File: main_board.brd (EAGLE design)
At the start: 100 x 80 mm, 60 parts, among them IC1 MBED_MICROCONTROLLER, J1 2060-402, U11 MC33887-HSOP, U13 MC33887-HSOP, U14 PCF8575PWE4, U2 SI8460AA-B-IS1, U3 MC33887-HSOP, U4 NFET-SOIC8, U5 LDO, U6 SI8460AA-B-IS1, U7 MC33887-HSOP, U8 SI8460AA-B-IS1, U9 MC33887-HSOP, X3 ENC1, X4 ENC2, X6 ENC3, X7 ENC4, X8 ENC5

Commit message: Major changes, nearly ready for first prototype
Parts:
- removed C3: 100nF, rcl:C0603K
- removed J1: 2060-402, Wago-2060-402:WAGO_2060-402
- removed JP1, JP3, JP4, JP5, JP6: MOTOR, SparkFun:SCREWTERMINAL-3.5MM-2
- removed JP2: PWR, SparkFun:SCREWTERMINAL-3.5MM-2
- removed LED4: (no value), led:CHIP-LED0603
- removed R19, R22, R25, R28: 10k, rcl:R0603
- removed U14: PCF8575PWE4, pcf8575:SOP65P640X120-24N
- removed U4: NFET-SOIC8, SparkFun:SO08
- removed U5: LDO, SparkFun:SOT23-5
- added BAT_12V, BAT_GND: (no value), tellis2:PWR_HOLE
- added BAT_15V, BAT_15V_GND, M1_1, M1_10, M1_2, M1_3, M1_4, M1_5, M1_6, M1_7, M1_8, M1_9: (no value), tellis2:WIRE_HOLE
- added LED1, LED2, LED3: (no value), led:CHIP-LED0603
- added R1, R2, R3, R4, R5: 10k, rcl:R0603
- added R14, R7, R8, R9: 2K2, rcl:R0603
- added U$1: V_REG_MIC2920, SparkFun-PowerIC:SOT223
- added U$2: MOSFET-N-SOT669, nxp_sot669:TO127P600X120-5N
- added U$3: D15V35F5S3, D15V35F5S3:D15V35F5S3
- added U1: PCA9555PW,118, PCA9555:SOP65P640X110-24N
- added X1: BALL_SENS, con-amp-micromatch:MICROMATCH-4
- added X10: IMU, con-amp-micromatch:MICROMATCH-4
- added X2: ETH, con-amp-micromatch:MICROMATCH-4
- added X5: BTNS, con-amp-micromatch:MICROMATCH-4
- added X9: COIL, con-amp-micromatch:MICROMATCH-6
- R11: value 10k -> 2K2
- R6: value 1k -> 2K2
- moved R11 176.1 mm to (77.7, 53.5), flipped to the bottom, turned to 180 degrees
- moved R29 155.1 mm to (49.3, 24.9), flipped to the bottom, turned to 90 degrees
- moved C30 151.2 mm to (36.6, 18.6)
- moved R6 144.5 mm to (95.5, 10.0), turned to 90 degrees
- moved C17 139.0 mm to (53.1, 27.2), turned to 270 degrees
- moved R27 137.9 mm to (36.6, 20.2), turned to 180 degrees
- moved R26 134.8 mm to (27.5, 7.31), flipped to the bottom, turned to 180 degrees
- moved C25 132.9 mm to (21.1, 21.2), turned to 270 degrees
- moved C16 131.4 mm to (54.4, 33.4)
- moved C6 130.7 mm to (37.3, 51.7), flipped to the bottom, turned to 270 degrees
- moved C8 130.0 mm to (27.1, 52.4), flipped to the bottom, turned to 270 degrees
- moved D1 128.9 mm to (27.8, 24.7), flipped to the bottom, turned to 180 degrees
- moved C5 123.9 mm to (48.6, 62.5), turned to 180 degrees
- moved R24 114.3 mm to (22.7, 21.3), turned to 90 degrees
- moved C20 113.9 mm to (21.1, 47.9), turned to 270 degrees
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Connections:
- removed net EXTEND_SCL: IC1.10, U14.22
- removed net EXTEND_SDA: IC1.9, U14.23
- removed net N$11: C3.1, U5.4
- removed net N$13: LED4.A, R6.1
- removed net N$17: R11.1, U3.20
- removed net N$32: R19.1, U7.20
- removed net N$37: R22.1, U9.20
- removed net N$42: R25.1, U11.20
- removed net N$47: R28.1, U13.20
- new net +15V: BAT_15V.P$1, U$3.EN, U$3.P$5
- new net BALL: U1.15, X1.2
- new net BTN1: U1.19, X5.2
- new net BTN2: U1.20, X5.4
- new net CHARGE: IC1.20, X9.4
- new net D+: IC1.31
- new net D-: IC1.32
- new net DONE: IC1.18, X9.5
- new net INT: IC1.8, R11.1, U1.1
- new net KICK: IC1.19, X9.3
- new net LED1: R6.2, U1.16
- new net LED2: R7.2, U1.17
- new net LED3: R8.2, U1.18
- new net N$19: X9.6
- new net N$2: R1.1, U3.20
- new net N$3: R2.1, U7.20
- new net N$4: R3.1, U13.20
- new net N$5: R4.1, U11.20
- new net N$6: R5.1, U9.20
- new net N$7: LED1.A, R6.1
- new net N$8: LED2.A, R7.1
- new net N$9: LED3.A, R8.1
- new net RD+: IC1.35, X2.2
- new net RD-: IC1.36, X2.1
- new net SCL: IC1.10, R9.1, U1.22, X10.3
- new net SDA: IC1.9, R14.1, U1.23, X10.4
- new net TD+: IC1.33, X2.4
- new net TD-: IC1.34, X2.3
- net +12V: now also U$1.1; no longer U5.1, U5.3
- net +3V3: now also R11.2, R14.2, R9.2, U1.24, X10.1; no longer U14.24
- net +5V: now also R1.2, R2.2, R3.2, R4.2, R5.2, U$1.3; no longer R11.2, R19.2, R22.2, R25.2, R28.2, R6.2, U5.5
- net DIR1_1: now also U1.5, U2.5; no longer U14.4, U2.3
- net DIR1_1_D: now also U2.12; no longer U2.14
- net DIR1_2: now also U1.4, U2.6; no longer U14.5, U2.4
- net DIR1_2_D: now also U2.11; no longer U2.13
- net DIR2_1: now also U1.7, U2.2; no longer U14.6, U2.6
- net DIR2_1_D: now also U2.15; no longer U2.11
- net DIR2_2: now also U1.6, U2.3; no longer U14.7, U2.7
- net DIR2_2_D: now also U2.14; no longer U2.10
- net DIR3_1: now also U1.9, U6.5; no longer U14.8, U6.3
- net DIR3_1_D: now also U6.12; no longer U6.14
- net DIR3_2: now also U1.8, U6.6; no longer U14.9, U6.4
- net DIR3_2_D: now also U6.11; no longer U6.13
- net DIR4_1: now also U1.11, U6.2; no longer U14.10, U6.6
- net DIR4_1_D: now also U6.15; no longer U6.11
- net DIR4_2: now also U1.10, U6.3; no longer U14.11, U6.7
- net DIR4_2_D: now also U6.14; no longer U6.10
- net DIR5_1: now also U1.13, U8.2; no longer U14.13, U8.3
- net DIR5_1_D: now also U8.15; no longer U8.14
- net DIR5_2: now also U1.14, U8.3; no longer U14.14, U8.4
- net DIR5_2_D: now also U8.14; no longer U8.13
- net ENC1A: now also IC1.5; no longer IC1.8
- net ENC1B: now also IC1.6; no longer IC1.11
- net ENC2A: now also IC1.7; no longer IC1.12
- net ENC2B: now also IC1.11; no longer IC1.15
- net ENC3A: now also IC1.12; no longer IC1.16
- net ENC3B: now also IC1.13; no longer IC1.17
- net ENC4A: now also IC1.14; no longer IC1.18
- net ENC4B: now also IC1.15; no longer IC1.26
- net ENC5A: now also IC1.16; no longer IC1.27
- net ENC5B: now also IC1.17; no longer IC1.28
- net GND: now also BAT_15V_GND.P$1, LED1.C, LED2.C, LED3.C, U$3.P$1, U$3.P$2, U$3.P$3, U$3.P$4, U1.12, U1.2, U1.21, U1.3, X1.1, X10.2, X5.1, X5.3, X9.1; no longer U14.12, U14.2, U14.21, U14.3
- net GNDA: now also U$1.2, U$1.4, U$2.1, U$2.2, U$2.3; no longer C3.2, LED4.C, U4.1, U4.2, U4.3, U5.2
- net N$20: now also U$2.4; no longer U4.4
- net N$21: now also BAT_GND.P$1, U$2.5; no longer JP2.1, U4.5, U4.6, U4.7, U4.8
- net N$23: now also M1_1.P$1; no longer JP1.2
- net N$25: now also M1_2.P$1; no longer JP1.1
- net N$30: now also BAT_12V.P$1; no longer JP2.2
- net N$34: now also M1_3.P$1; no longer JP3.2
- net N$35: now also M1_4.P$1; no longer JP3.1
- net N$39: now also M1_5.P$1; no longer JP4.2
- net N$40: now also M1_6.P$1; no longer JP4.1
- net N$44: now also M1_7.P$1; no longer JP5.2
- net N$45: now also M1_8.P$1; no longer JP5.1
- net N$49: now also M1_9.P$1; no longer JP6.2
- net N$50: now also M1_10.P$1; no longer JP6.1
- net PWM1: now also IC1.25, U2.7; no longer IC1.21, U2.2
- net PWM1_D: now also U2.10; no longer U2.15
- net PWM2: now also IC1.24, U2.4; no longer IC1.22, U2.5
- net PWM2_D: now also U2.13; no longer U2.12
- net PWM3: now also U6.7; no longer U6.2
- net PWM3_D: now also U6.10; no longer U6.15
- net PWM4: now also IC1.22, U6.4; no longer IC1.24, U6.5
- net PWM4_D: now also U6.13; no longer U6.12
- net PWM5: now also IC1.21, U8.4; no longer IC1.25, U8.2
- net PWM5_D: now also U8.13; no longer U8.15
- net VCC: now also U$3.P$7, U$3.P$8, X1.3, X9.2
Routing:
- net VCC: track 0.00 -> 161.8 mm
- net +5V: track 0.00 -> 148.0 mm, vias 0 -> 3
- net +12V: track 0.00 -> 135.5 mm
- net +3V3: track 0.00 -> 95.1 mm, vias 0 -> 1
- net PWM3: track 0.00 -> 77.7 mm, vias 0 -> 2
- net PWM4: track 0.00 -> 75.6 mm, vias 0 -> 2
- net PWM2: track 0.00 -> 73.9 mm, vias 0 -> 2
- net PWM1: track 0.00 -> 70.8 mm, vias 0 -> 2
- net PWM5: track 0.00 -> 70.6 mm, vias 0 -> 2
- net BTN1: track 0.00 -> 57.8 mm
- net LED1: track 0.00 -> 55.3 mm
- net LED3: track 0.00 -> 54.8 mm
- net LED2: track 0.00 -> 54.1 mm
- net BTN2: track 0.00 -> 54.1 mm
- net SCL: track 0.00 -> 53.2 mm
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- added copper zone on layer 16, net +12V
- added copper zone on layer 1, net GND
- added copper zone on layer 16, net GND
- added copper zone on layer 1, net GNDA
- added copper zone on layer 16, net GNDA
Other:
- outline, holes or cut-outs redrawn

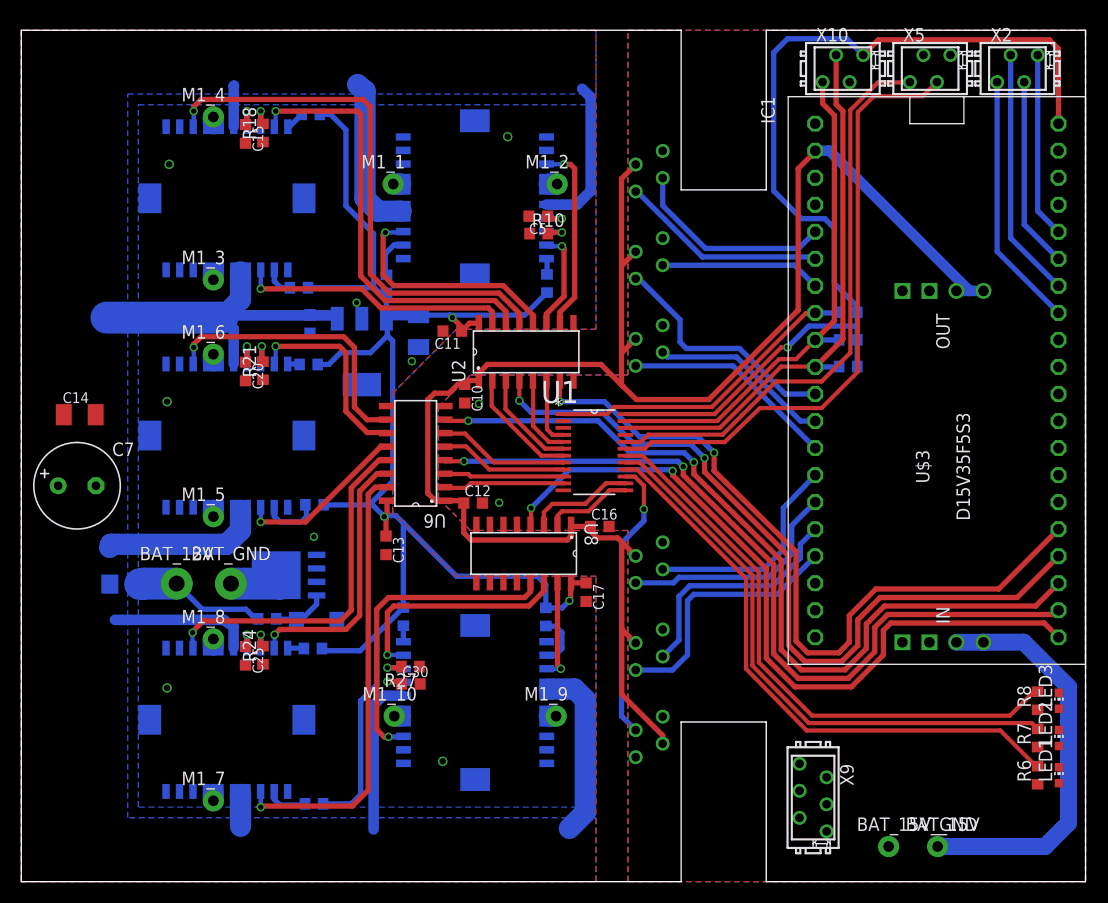
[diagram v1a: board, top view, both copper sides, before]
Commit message: Improved board layout
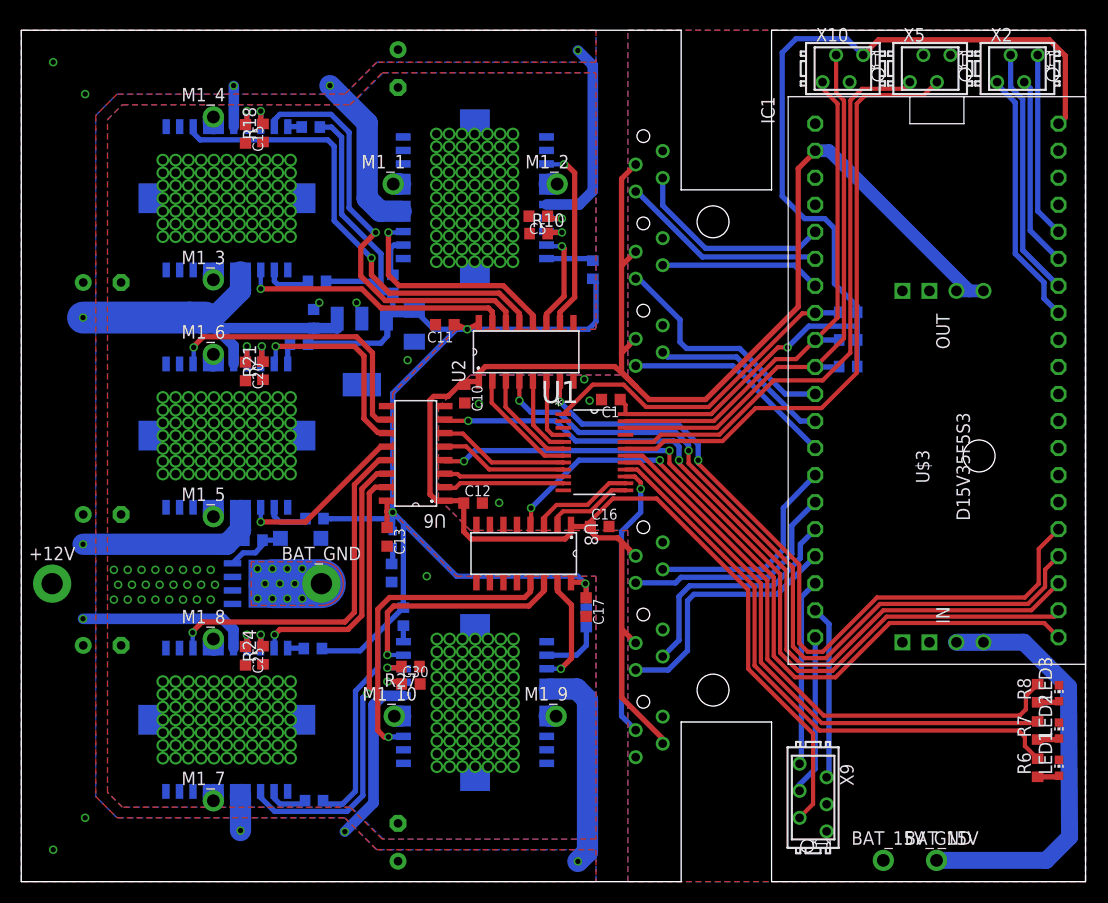
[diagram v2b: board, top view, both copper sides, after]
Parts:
- removed BAT_12V: (no value), tellis2:PWR_HOLE
- removed C14: 10uF, rcl:C1206K
- removed F3: FUSE_5A, rcl:R1206
- added +12V: (no value), tellis2:PWR_HOLE
- added C1: 100nF, rcl:C0603K
- added C2, C3, C4, C9: 470uF, rcl:E3,5-8
- added LED4: (no value), led:CHIP-LED0603
- added R15: 2K2, rcl:R0603
- C7: value 470uF-16V -> 470uF
- U$2: value MOSFET-N-SOT669 -> MOSFET-N
- moved BAT_GND 8.50 mm to (28.2, 28.0)
- moved D1 7.75 mm to (26.2, 32.3)
- moved R13 7.51 mm to (21.8, 32.1)
- moved R1 4.49 mm to (53.7, 57.5)
- moved R29 3.80 mm to (53.1, 24.8)
- moved C7 3.59 mm to (7.60, 34.5), flipped to the bottom, turned to 180 degrees
- moved U$2 2.72 mm to (22.5, 28.0), turned to 180 degrees
- moved R5 2.10 mm to (26.1, 50.5)
- moved R20 1.80 mm to (27.8, 56.4)
- moved C17 1.40 mm to (53.1, 25.8)
- moved BAT_15V_GND 1.39 mm to (81.0, 2.00)
- moved BAT_15V 1.30 mm to (86.0, 2.00)
- moved R23 1.30 mm to (27.6, 34.1)
- moved R2 1.20 mm to (27.2, 70.9)
- moved C11 0.92 mm to (39.8, 52.3)
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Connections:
- removed net D+: IC1.31
- removed net D-: IC1.32
- removed net N$19: X9.6
- removed net N$30: BAT_12V.P$1, C14.1, C7.+, F3.2, R13.2
- new net N$10: LED4.A, R15.2
- net +12V: now also +12V.P$1, C2.+, C3.+, C4.+, C7.+, C9.+, R13.2; no longer F3.1
- net +3V3: now also C1.1
- net +5V: now also LED4.C
- net CHARGE: now also IC1.19, X9.5; no longer IC1.20, X9.4
- net DONE: now also X9.6; no longer X9.5
- net GND: now also C1.2
- net GNDA: now also C2.-, C3.-, C4.-, C9.-, R15.1; no longer C14.2
- net KICK: now also IC1.20, X9.4; no longer IC1.19, X9.3
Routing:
- net VCC: track 161.8 -> 205.8 mm
- net +12V: track 135.5 -> 159.6 mm, vias 0 -> 13
- net DONE: track 0.00 -> 17.6 mm
- net CHARGE: track 0.00 -> 16.3 mm
- net KICK: track 0.00 -> 15.1 mm
- net N$30: track 12.5 -> 0.00 mm
- net +5V: track 148.0 -> 159.1 mm
- net PWM2_D: track 51.2 -> 44.3 mm
- net N$2: track 1.52 -> 4.78 mm
- net N$8: track 0.00 -> 2.10 mm
- net N$7: track 0.00 -> 2.10 mm
- net N$9: track 0.00 -> 2.10 mm
- net PWM3: track 77.7 -> 75.7 mm
- net PWM5: track 70.6 -> 68.7 mm
- net FAULT1_D: track 2.78 -> 4.57 mm
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- added copper zone on layer 1, net +12V
- added copper zone on layer 1, net N$21
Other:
- outline, holes or cut-outs redrawn

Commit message: Added some labels and vias
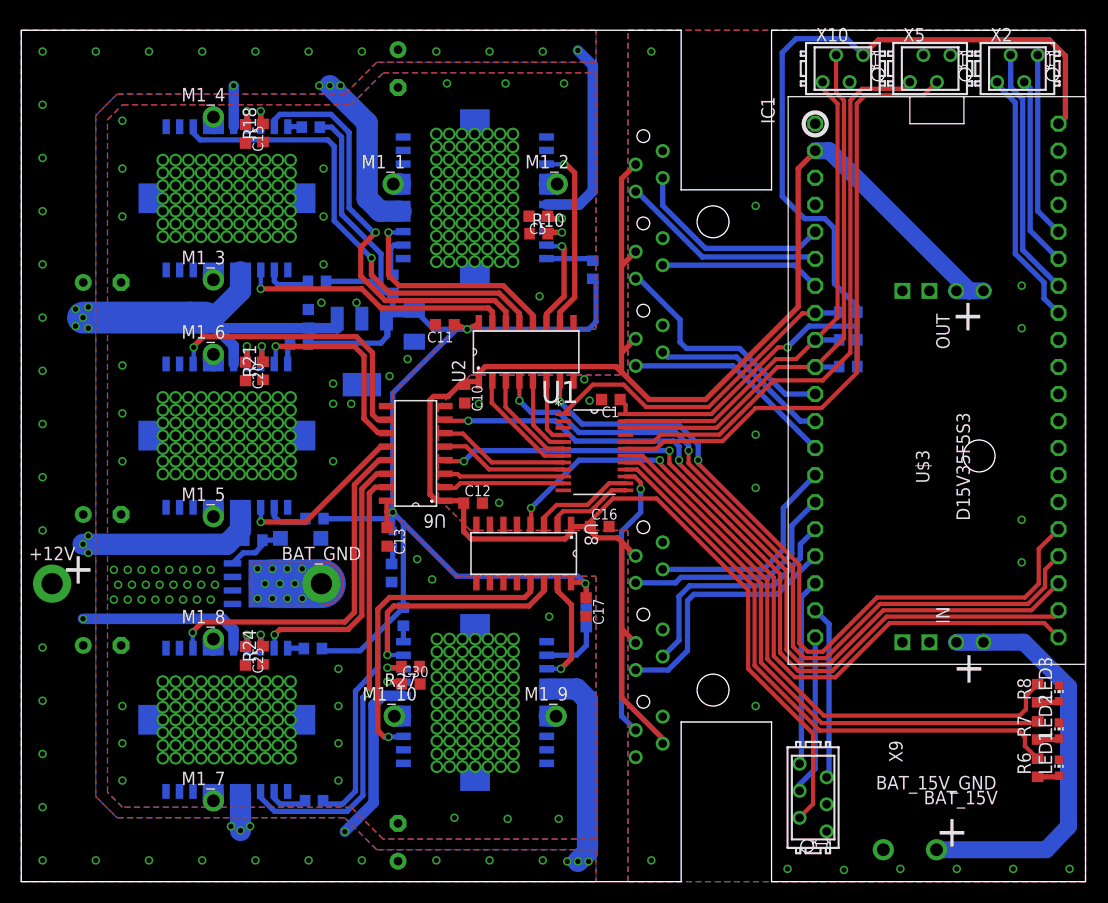
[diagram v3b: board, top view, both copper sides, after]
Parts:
- moved BAT_15V 1.00 mm to (86.0, 3.00)
- moved BAT_15V_GND 1.00 mm to (81.0, 3.00)
- moved C8 0.50 mm to (27.0, 52.9)
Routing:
- net VCC: track 205.8 -> 204.0 mm
- net +15V: track 39.8 -> 38.7 mm
- net +12V: track 159.6 -> 160.1 mm, vias 13 -> 54
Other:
- board text added: "+"
- board text added: "M1"
- board text added: "M2"
- board text added: "M3"
- board text added: "M4"
- board text added: "M5"

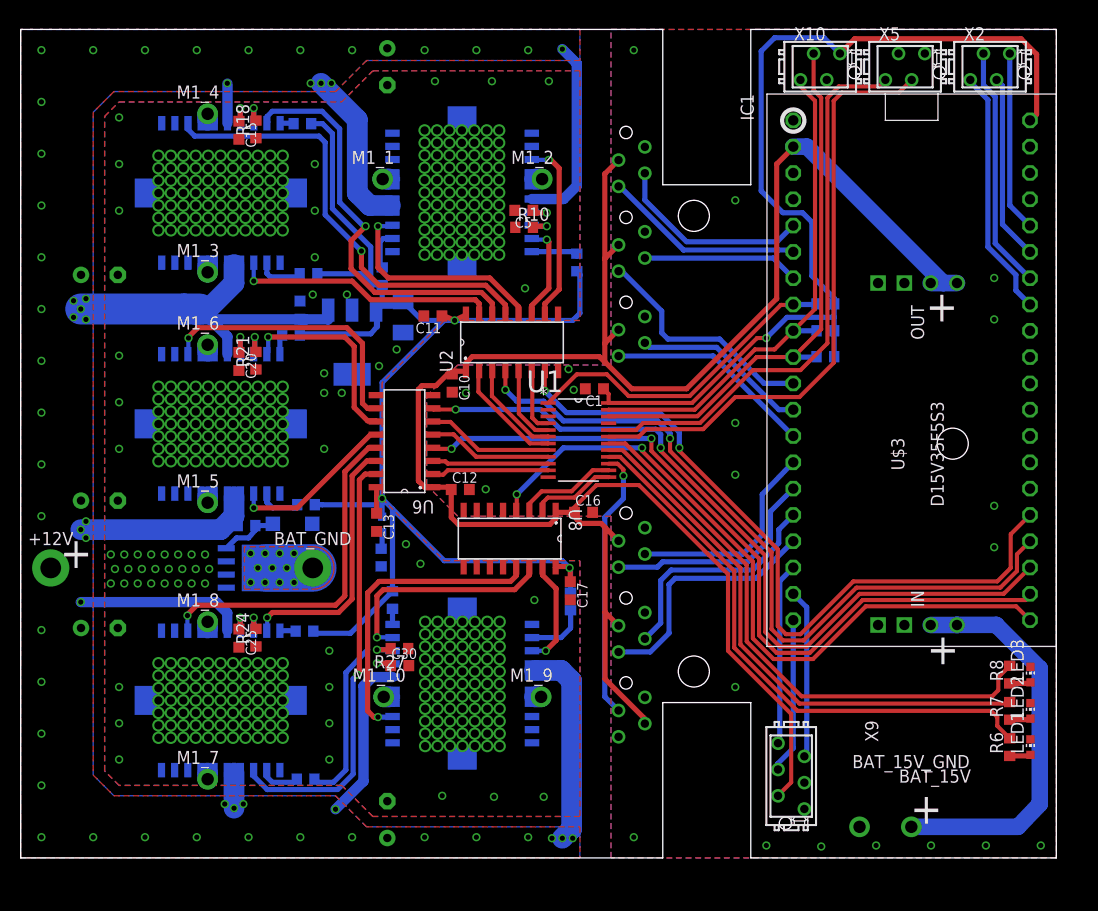
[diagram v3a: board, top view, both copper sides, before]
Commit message: Added capacitor to buttons, switched IMU and buttons connector positions, moved voltage regulator to better position, connected IMU connector to second I2C pins added pull-down resistors to PWM pins, added pull-up resitor to kick pin, added pull-down resistor to charge pin, made wire holes a bit bigger
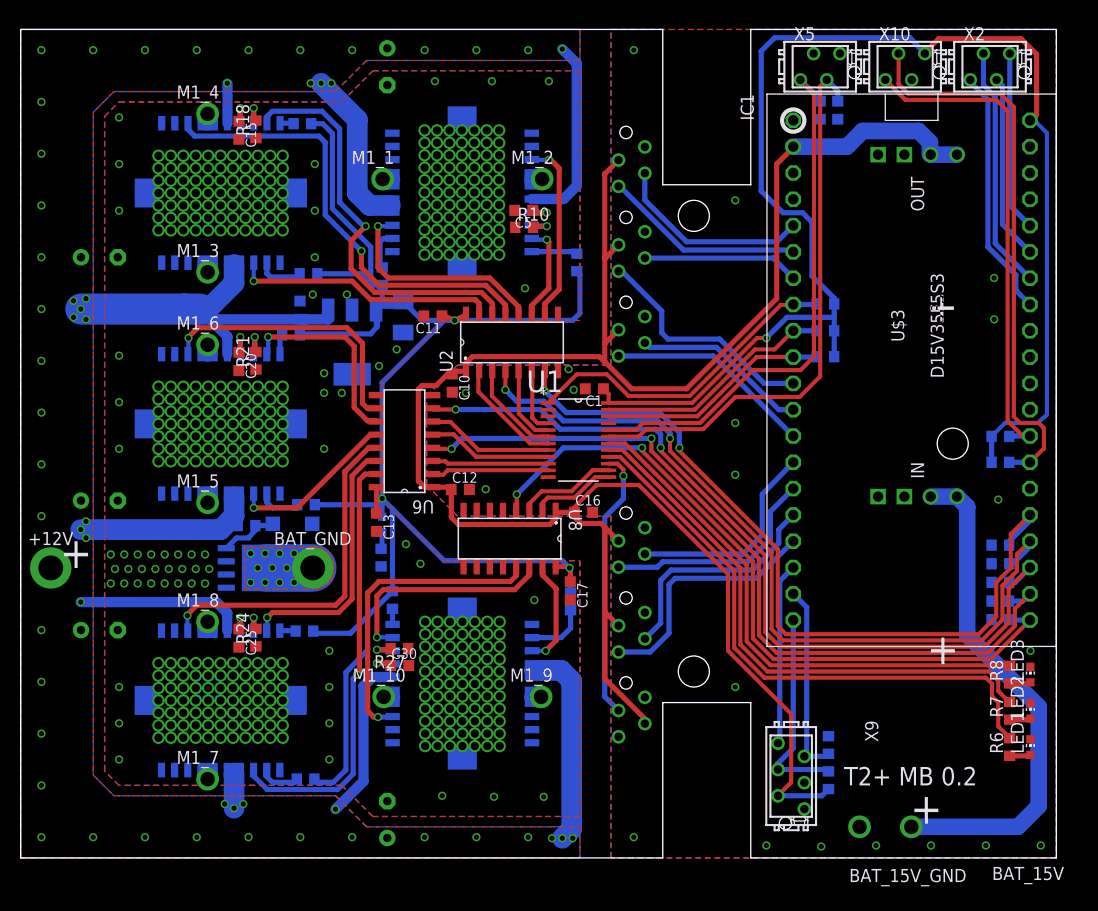
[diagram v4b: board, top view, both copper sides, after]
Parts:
- added C14, C18: 100nF, rcl:C0603K
- added R16, R17, R19, R22, R25, R28, R30: 10k, rcl:R0603
- added R31, R32: 2K2, rcl:R0603
- moved U$3 12.4 mm to (86.6, 51.4)
- moved X10 8.20 mm to (85.4, 76.4)
- moved X5 8.20 mm to (77.2, 76.4)
- moved C3 1.70 mm to (7.60, 58.0)
- moved C2 0.20 mm to (7.60, 22.0)
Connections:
- new net SCL2: IC1.27, R32.1, X10.3
- new net SDA2: IC1.28, R31.1, X10.4
- net +3V3: now also R31.2, R32.2
- net BTN1: now also C14.1
- net BTN2: now also C18.1
- net CHARGE: now also R17.2
- net GND: now also C14.2, C18.2, R17.1, R19.1, R22.1, R25.1, R28.1, R30.1
- net KICK: now also R16.1
- net PWM1: now also R30.2
- net PWM2: now also R28.2
- net PWM3: now also R25.2
- net PWM4: now also R22.2
- net PWM5: now also R19.2
- net SCL: no longer X10.3
- net SDA: no longer X10.4
- net VCC: now also R16.2
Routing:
- net SCL2: track 0.00 -> 54.1 mm
- net SDA2: track 0.00 -> 47.8 mm
- net +3V3: track 96.0 -> 134.1 mm
- net SCL: track 53.2 -> 22.5 mm
- net SDA: track 48.9 -> 23.2 mm
- net +15V: track 38.7 -> 48.8 mm
- net PWM1: track 70.7 -> 76.3 mm
- net PWM2: track 72.8 -> 78.0 mm
- net KICK: track 15.1 -> 20.0 mm
- net PWM3: track 75.7 -> 80.2 mm
- net BTN1: track 58.4 -> 54.2 mm
- net PWM4: track 74.2 -> 77.4 mm
- net LED3: track 55.5 -> 52.4 mm
- net CHARGE: track 16.3 -> 18.8 mm
- net BTN2: track 54.6 -> 52.9 mm
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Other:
- board text added: "T2+ MB 0.2"
